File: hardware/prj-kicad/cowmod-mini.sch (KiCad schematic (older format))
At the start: 2 parts, among them P1 PMOD, P2 PMOD

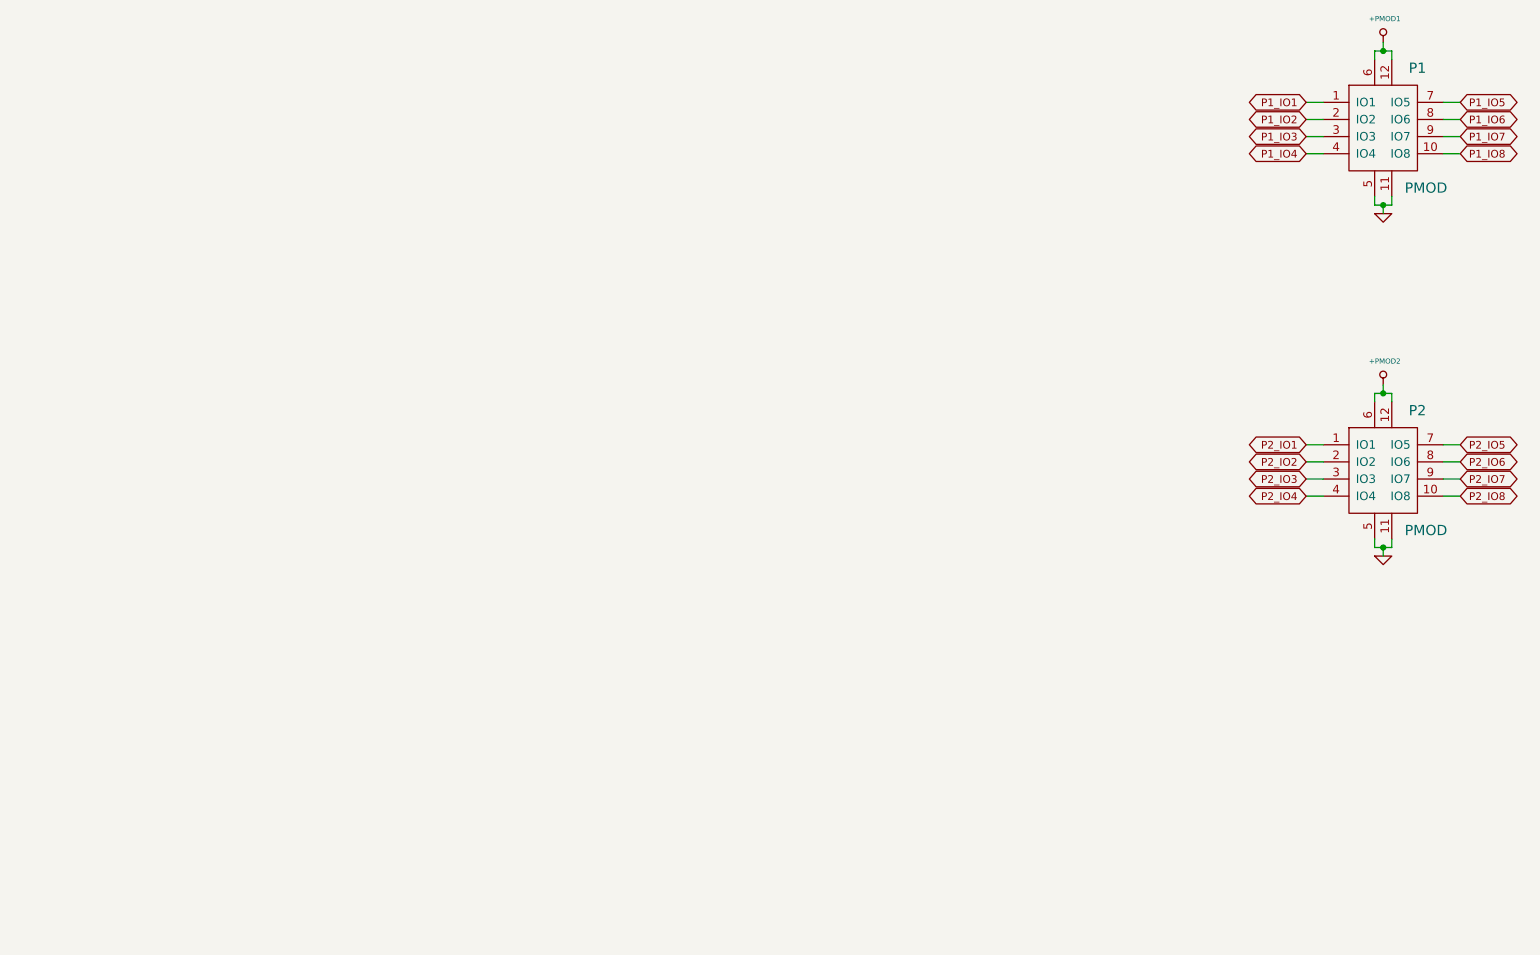
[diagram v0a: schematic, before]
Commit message: = ADD: Insert FPGA to drive external PMOD interfaces
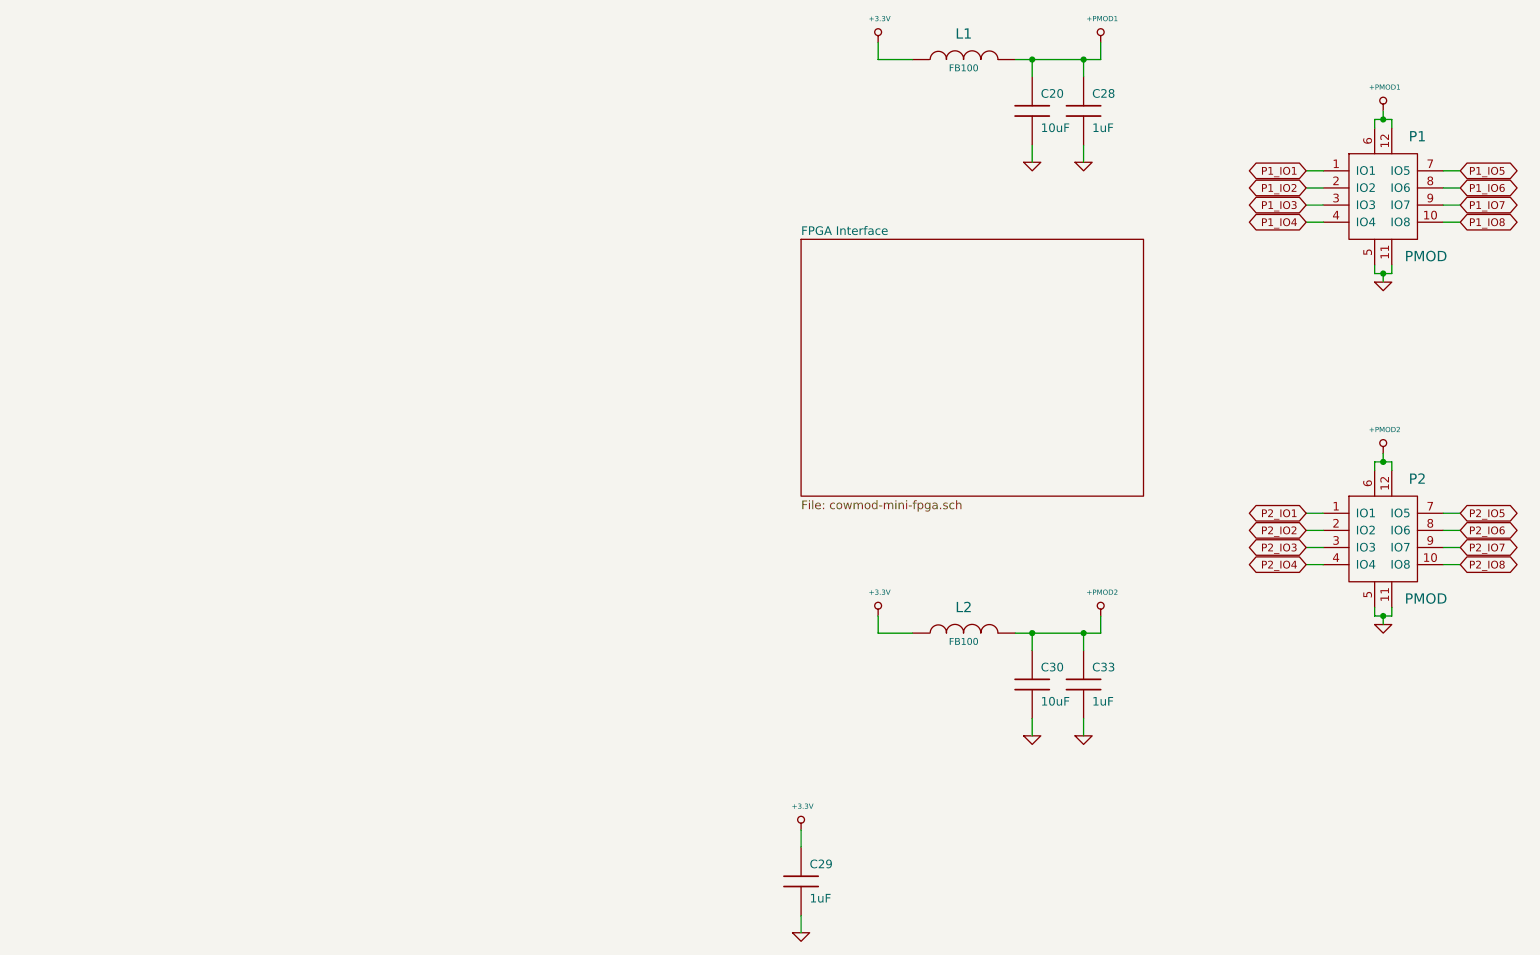
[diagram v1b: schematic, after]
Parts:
- added C20, C30: 10uF, cowmod-mini:SMD1206, symbol cowmod-mini:C
- added C28, C29, C33: 1uF, cowmod-mini:SMD0603, symbol cowmod-mini:C
- added L1, L2: FB100, cowmod-mini:SMD0805, symbol cowmod-mini:INDUCTOR
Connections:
- net +PMOD1: now also C20.1, C28.1, L1.2
- net +PMOD2: now also C30.1, C33.1, L2.2
- net GND: now also C20.2, C28.2, C29.2, C30.2, C33.2
- new net +3.3V: C29.1, L1.1, L2.1
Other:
- moved on the sheet: P1, P2

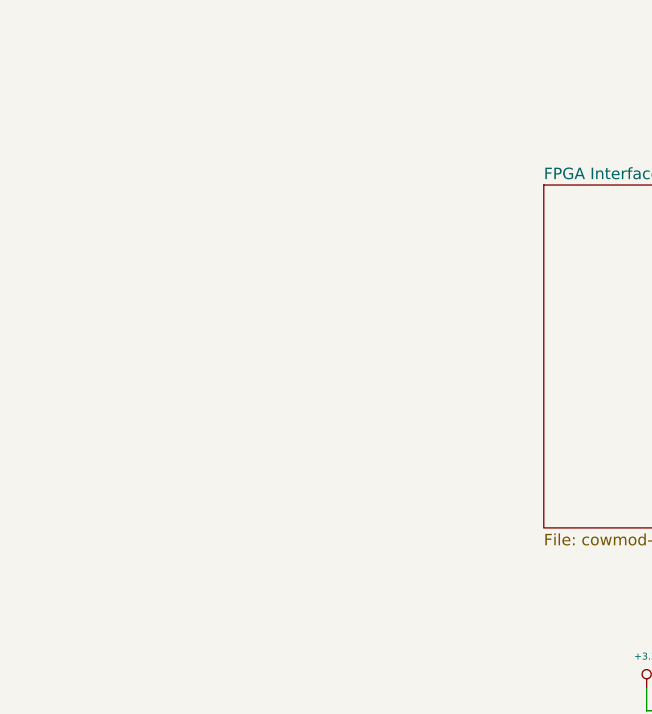
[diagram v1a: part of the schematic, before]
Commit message: = ADD: Insert MCU and connect it to FPGA
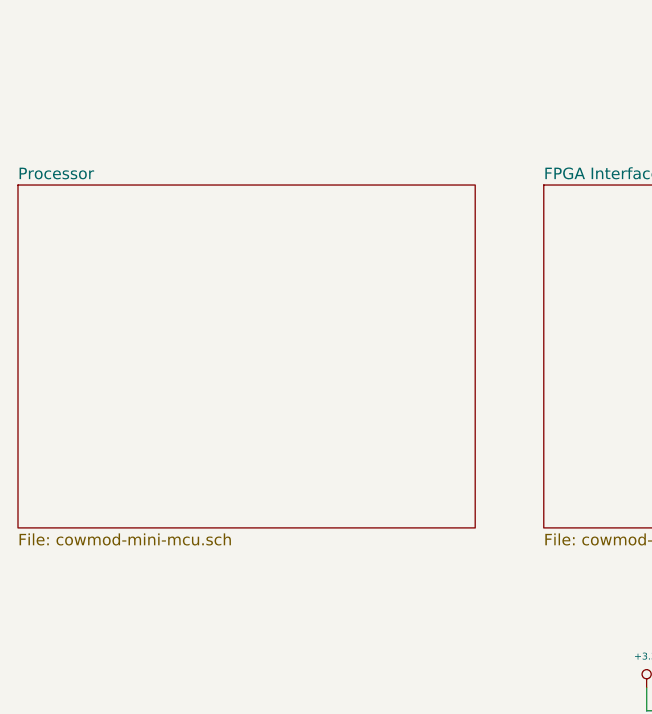
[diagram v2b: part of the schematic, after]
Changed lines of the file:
@@
 $Descr A4 11693 8268
 encoding utf-8
-Sheet 1 2
+Sheet 1 3
 Title "Cowmod Mini"
 Date "2020-02-03"
@@
 $Comp
 L cowmod-mini:+3.3V #PWR0123
-U 1 1 5E38F113
+U 1 1 5E3A50A3
 P 6750 1450
 F 0 "#PWR0123" H 6750 1410 30  0001 C CNN
@@
 $Comp
 L cowmod-mini:INDUCTOR L1
-U 1 1 5E38FD78
+U 1 1 5E3A5D08
 P 7250 1550
 F 0 "L1" V 7400 1550 60  0000 C CNN
@@
 $Comp
 L cowmod-mini:C C20
-U 1 1 5E3904BB
+U 1 1 5E3A644B
 P 7650 1850
 F 0 "C20" H 7700 1950 50  0000 L CNN
@@
 $Comp
 L cowmod-mini:GND #PWR0124
-U 1 1 5E390512
+U 1 1 5E3A64A2
 P 7650 2150
 F 0 "#PWR0124" H 7650 2150 30  0001 C CNN
@@
 $Comp
 L cowmod-mini:+PMOD1 #PWR0125
-U 1 1 5E391339
+U 1 1 5E3A72C9
 P 8050 1450
 F 0 "#PWR0125" H 8050 1410 30  0001 C CNN
@@
 $Comp
 L cowmod-mini:C C28
-U 1 1 5E39A414
+U 1 1 5E3B03A4
 P 7950 1850
 F 0 "C28" H 8000 1950 50  0000 L CNN
@@
 $Comp
 L cowmod-mini:GND #PWR0138
-U 1 1 5E39DA34
+U 1 1 5E3B39C4
 P 7950 2150
 F 0 "#PWR0138" H 7950 2150 30  0001 C CNN
@@
 $Comp
 L cowmod-mini:C C33
-U 1 1 5E39DAD8
+U 1 1 5E3B3A68
 P 7950 5200
 F 0 "C33" H 8000 5300 50  0000 L CNN
@@
 $Comp
 L cowmod-mini:GND #PWR0139
-U 1 1 5E39DAE9
+U 1 1 5E3B75E8
 P 7950 5500
 F 0 "#PWR0139" H 7950 5500 30  0001 C CNN
@@
 	1    0    0    -1
 $EndComp
+$Sheet
+S 4000 2600 2000 1500
+U 5E3AB11B
+F0 "Processor" 50
+F1 "cowmod-mini-mcu.sch" 50
+$EndSheet
 $EndSCHEMATC

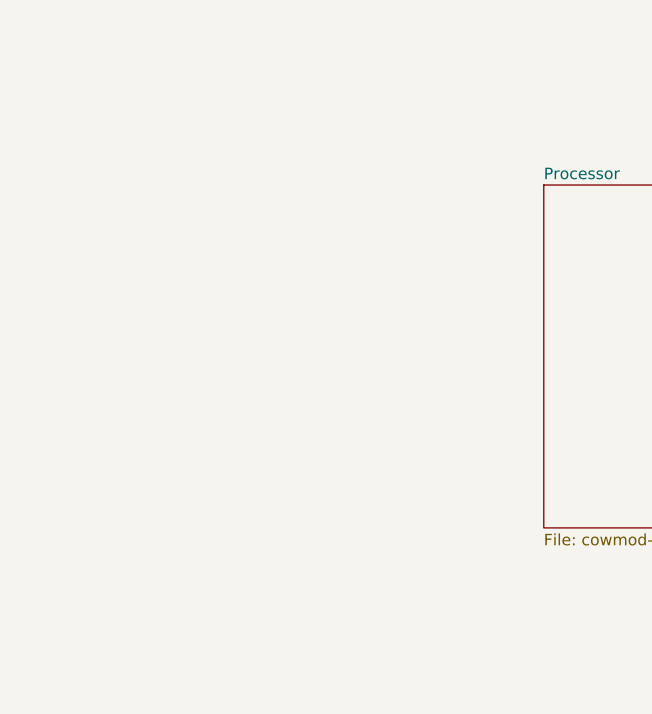
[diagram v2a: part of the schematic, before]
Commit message: = ADD: Insert ethernet network interface
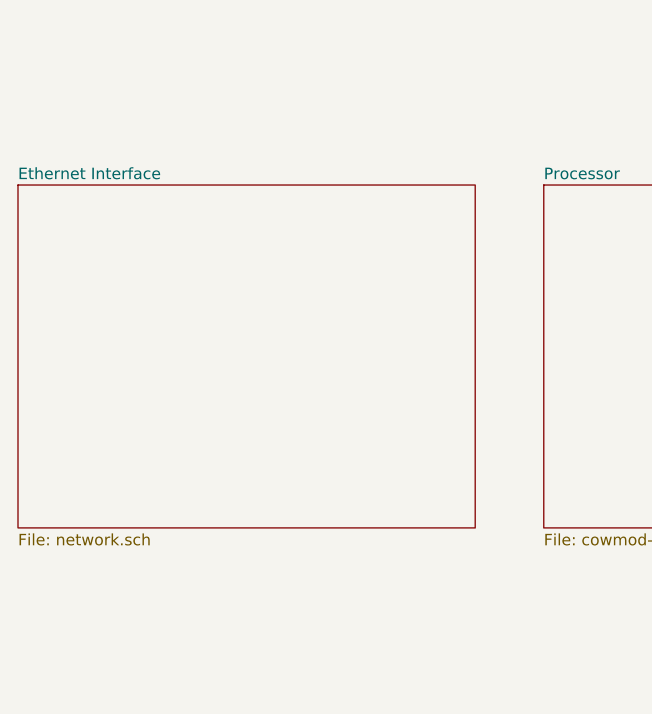
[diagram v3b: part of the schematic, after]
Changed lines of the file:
@@
 $Descr A4 11693 8268
 encoding utf-8
-Sheet 1 3
+Sheet 1 4
 Title "Cowmod Mini"
 Date "2020-02-03"
@@
 F1 "cowmod-mini-mcu.sch" 50
 $EndSheet
+$Sheet
+S 1700 2600 2000 1500
+U 5E3BE106
+F0 "Ethernet Interface" 50
+F1 "network.sch" 50
+$EndSheet
 $EndSCHEMATC

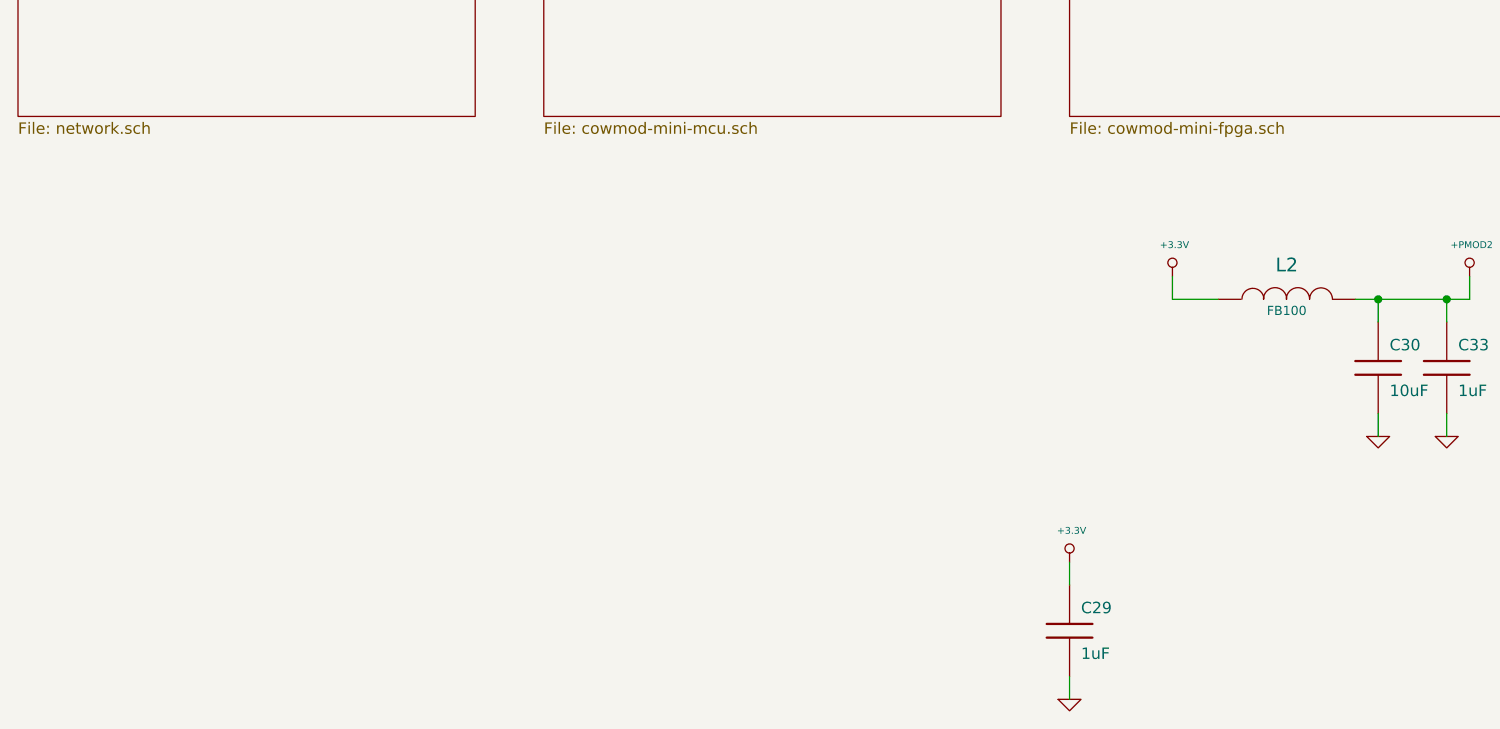
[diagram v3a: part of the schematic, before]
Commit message: = ADD: Insert power supply regulators (3V3 / 1V2 / 2V5)
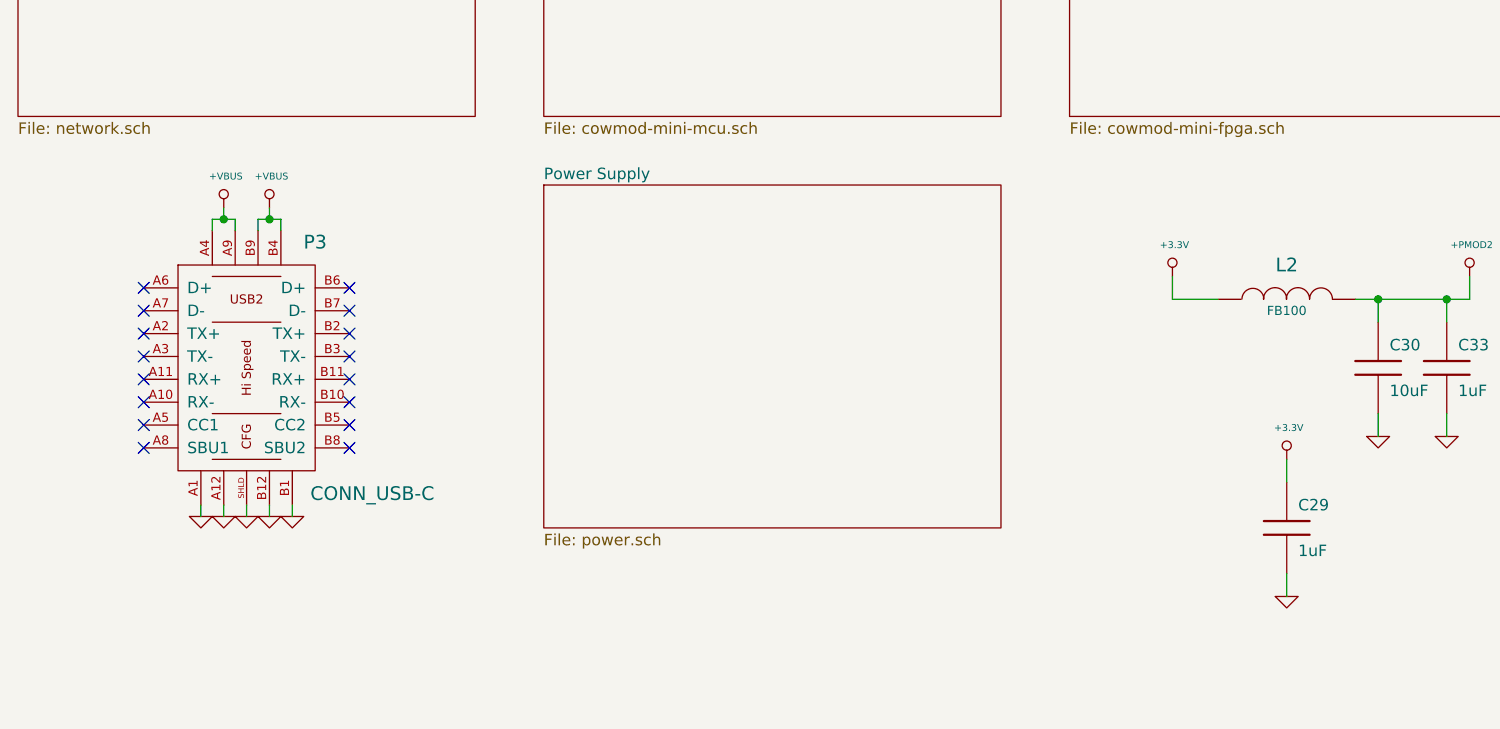
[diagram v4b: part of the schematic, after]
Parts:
- added P3: CONN_USB-C, cowmod-mini:CONN_632723300011, symbol cowmod-mini:CONN_USB-C
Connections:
- net GND: now also P3.A1, P3.A12, P3.B1, P3.B12, P3.SHLD
- new net +VBUS: P3.A4, P3.A9, P3.B4, P3.B9
- no-connect marks 0 -> 16
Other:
- moved on the sheet: C29
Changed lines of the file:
@@
 $Descr A4 11693 8268
 encoding utf-8
-Sheet 1 4
+Sheet 1 5
 Title "Cowmod Mini"
 Date "2020-02-03"
@@
 L cowmod-mini:+3.3V #PWR0129
 U 1 1 5E3979BD
-P 6300 6050
-F 0 "#PWR0129" H 6300 6010 30  0001 C CNN
-F 1 "+3.3V" H 6309 6188 30  0000 C CNN
-F 2 "" H 6300 6050 60  0000 C CNN
-F 3 "" H 6300 6050 60  0000 C CNN
-	1    6300 6050
+P 7250 5600
+F 0 "#PWR0129" H 7250 5560 30  0001 C CNN
+F 1 "+3.3V" H 7259 5738 30  0000 C CNN
+F 2 "" H 7250 5600 60  0000 C CNN
+F 3 "" H 7250 5600 60  0000 C CNN
+	1    7250 5600
 	1    0    0    -1
 $EndComp
@@
 L cowmod-mini:C C29
 U 1 1 5E397A10
-P 6300 6350
-F 0 "C29" H 6350 6450 50  0000 L CNN
-F 1 "1uF" H 6350 6250 50  0000 L CNN
-F 2 "cowmod-mini:SMD0603" H 6300 6350 60  0001 C CNN
-F 3 "" H 6300 6350 60  0000 C CNN
-	1    6300 6350
+P 7250 5900
+F 0 "C29" H 7300 6000 50  0000 L CNN
+F 1 "1uF" H 7300 5800 50  0000 L CNN
+F 2 "cowmod-mini:SMD0603" H 7250 5900 60  0001 C CNN
+F 3 "" H 7250 5900 60  0000 C CNN
+	1    7250 5900
 	1    0    0    -1
 $EndComp
@@
 L cowmod-mini:GND #PWR0130
 U 1 1 5E397B27
-P 6300 6650
-F 0 "#PWR0130" H 6300 6650 30  0001 C CNN
-F 1 "GND" H 6300 6580 30  0001 C CNN
-F 2 "" H 6300 6650 60  0000 C CNN
-F 3 "" H 6300 6650 60  0000 C CNN
-	1    6300 6650
-	1    0    0    -1
-$EndComp
-Wire Wire Line
-	6300 6650 6300 6550
-Wire Wire Line
-	6300 6150 6300 6050
+P 7250 6200
+F 0 "#PWR0130" H 7250 6200 30  0001 C CNN
+F 1 "GND" H 7250 6130 30  0001 C CNN
+F 2 "" H 7250 6200 60  0000 C CNN
+F 3 "" H 7250 6200 60  0000 C CNN
+	1    7250 6200
+	1    0    0    -1
+$EndComp
+Wire Wire Line
+	7250 6200 7250 6100
+Wire Wire Line
+	7250 5700 7250 5600
 $Comp
 L cowmod-mini:C C28
@@
 F1 "network.sch" 50
 $EndSheet
+$Comp
+L cowmod-mini:CONN_USB-C P3
+U 1 1 5E3E8043
+P 2700 5200
+F 0 "P3" H 3000 5750 60  0000 C CNN
+F 1 "CONN_USB-C" H 3250 4650 60  0000 C CNN
+F 2 "cowmod-mini:CONN_632723300011" H 2700 5200 60  0001 C CNN
+F 3 "" H 2700 5200 60  0000 C CNN
+	1    2700 5200
+	1    0    0    -1
+$EndComp
+$Comp
+L cowmod-mini:GND #PWR0172
+U 1 1 5E3E8206
+P 2500 5850
+F 0 "#PWR0172" H 2500 5850 30  0001 C CNN
+F 1 "GND" H 2500 5780 30  0001 C CNN
+F 2 "" H 2500 5850 60  0000 C CNN
+F 3 "" H 2500 5850 60  0000 C CNN
+	1    2500 5850
+	1    0    0    -1
+$EndComp
+$Comp
+L cowmod-mini:GND #PWR0173
+U 1 1 5E3E8246
+P 2600 5850
+F 0 "#PWR0173" H 2600 5850 30  0001 C CNN
+F 1 "GND" H 2600 5780 30  0001 C CNN
+F 2 "" H 2600 5850 60  0000 C CNN
+F 3 "" H 2600 5850 60  0000 C CNN
+	1    2600 5850
+	1    0    0    -1
+$EndComp
+$Comp
+L cowmod-mini:GND #PWR0174
+U 1 1 5E3E8286
+P 2800 5850
+F 0 "#PWR0174" H 2800 5850 30  0001 C CNN
+F 1 "GND" H 2800 5780 30  0001 C CNN
+F 2 "" H 2800 5850 60  0000 C CNN
+F 3 "" H 2800 5850 60  0000 C CNN
+	1    2800 5850
+	1    0    0    -1
+$EndComp
+$Comp
+L cowmod-mini:GND #PWR0175
+U 1 1 5E3E82C6
+P 2900 5850
+F 0 "#PWR0175" H 2900 5850 30  0001 C CNN
+F 1 "GND" H 2900 5780 30  0001 C CNN
+F 2 "" H 2900 5850 60  0000 C CNN
+F 3 "" H 2900 5850 60  0000 C CNN
+	1    2900 5850
+	1    0    0    -1
+$EndComp
+Wire Wire Line
+	2900 5850 2900 5800
+Wire Wire Line
+	2800 5850 2800 5800
+Wire Wire Line
+	2600 5850 2600 5800
+Wire Wire Line
+	2500 5850 2500 5800
+$Comp
+L cowmod-mini:+VBUS #PWR0176
+U 1 1 5E3EE267
+P 2600 4500
+F 0 "#PWR0176" H 2600 4460 30  0001 C CNN
+F 1 "+VBUS" H 2609 4638 30  0000 C CNN
+F 2 "" H 2600 4500 60  0000 C CNN
+F 3 "" H 2600 4500 60  0000 C CNN
+	1    2600 4500
+	1    0    0    -1
+$EndComp
+$Comp
+L cowmod-mini:+VBUS #PWR0177
+U 1 1 5E3EE2A7
+P 2800 4500
+F 0 "#PWR0177" H 2800 4460 30  0001 C CNN
+F 1 "+VBUS" H 2809 4638 30  0000 C CNN
+F 2 "" H 2800 4500 60  0000 C CNN
+F 3 "" H 2800 4500 60  0000 C CNN
+	1    2800 4500
+	1    0    0    -1
+$EndComp
+Wire Wire Line
+	2800 4500 2800 4550
+Wire Wire Line
+	2800 4550 2750 4550
+Wire Wire Line
+	2750 4550 2750 4600
+Wire Wire Line
+	2800 4550 2850 4550
+Wire Wire Line
+	2850 4550 2850 4600
+Connection ~ 2800 4550
+Wire Wire Line
+	2650 4600 2650 4550
+Wire Wire Line
+	2650 4550 2600 4550
+Wire Wire Line
+	2550 4550 2550 4600
+Wire Wire Line
+	2600 4500 2600 4550
+Connection ~ 2600 4550
+Wire Wire Line
+	2600 4550 2550 4550
+NoConn ~ 2250 4850
+NoConn ~ 2250 4950
+NoConn ~ 2250 5050
+NoConn ~ 2250 5150
+NoConn ~ 2250 5250
+NoConn ~ 2250 5350
+NoConn ~ 2250 5450
+NoConn ~ 2250 5550
+NoConn ~ 3150 4850
+NoConn ~ 3150 4950
+NoConn ~ 3150 5050
+NoConn ~ 3150 5150
+NoConn ~ 3150 5250
+NoConn ~ 3150 5350
+NoConn ~ 3150 5450
+NoConn ~ 3150 5550
+$Sheet
+S 4000 4400 2000 1500
+U 5E411700
+F0 "Power Supply" 50
+F1 "power.sch" 50
+$EndSheet
+$Comp
+L cowmod-mini:GND #PWR0178
+U 1 1 5E41EA90
+P 2700 5850
+F 0 "#PWR0178" H 2700 5850 30  0001 C CNN
+F 1 "GND" H 2700 5780 30  0001 C CNN
+F 2 "" H 2700 5850 60  0000 C CNN
+F 3 "" H 2700 5850 60  0000 C CNN
+	1    2700 5850
+	1    0    0    -1
+$EndComp
+Wire Wire Line
+	2700 5850 2700 5800
 $EndSCHEMATC
